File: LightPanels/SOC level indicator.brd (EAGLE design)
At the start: 170 x 162.3 mm, 156 parts

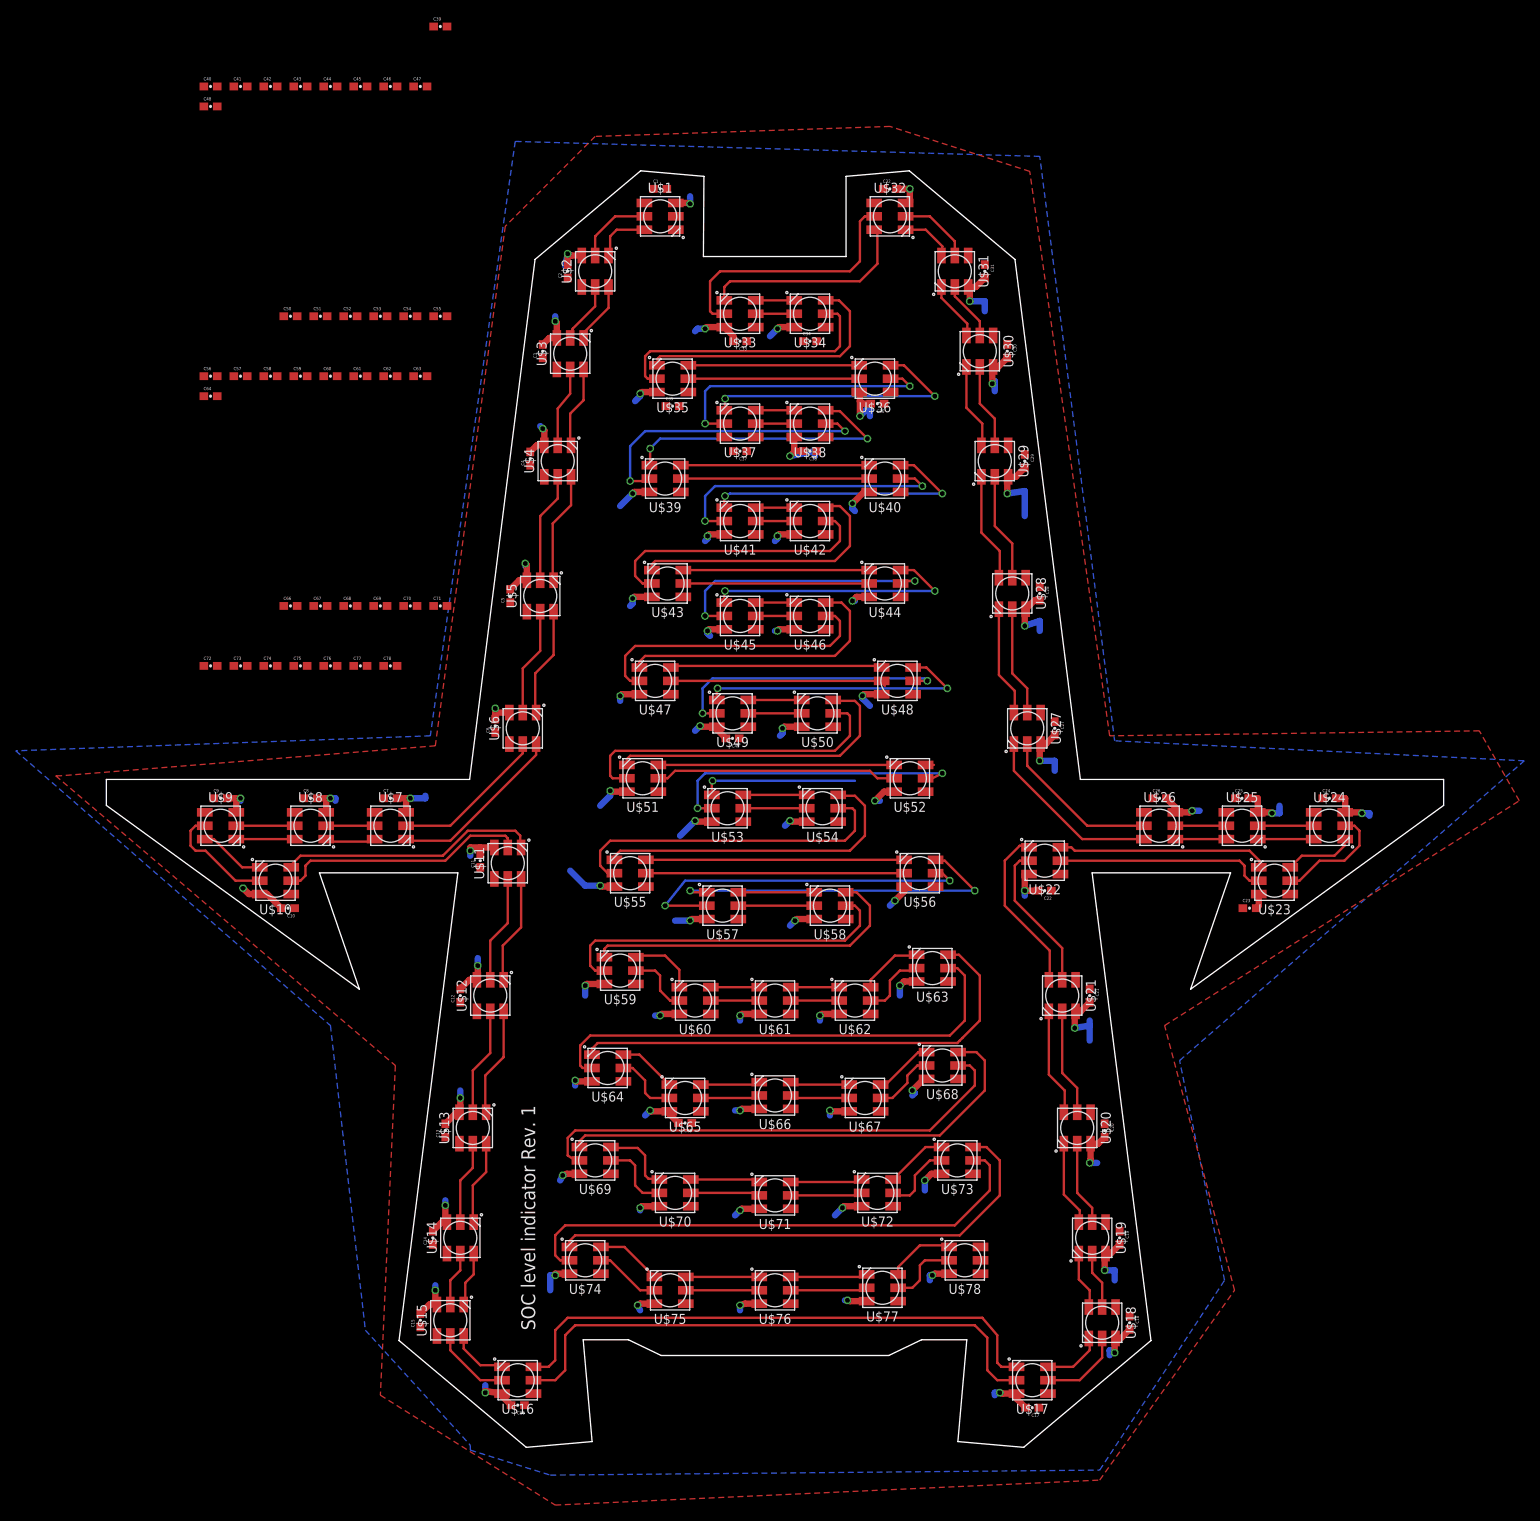
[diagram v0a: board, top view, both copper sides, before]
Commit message: No airwires
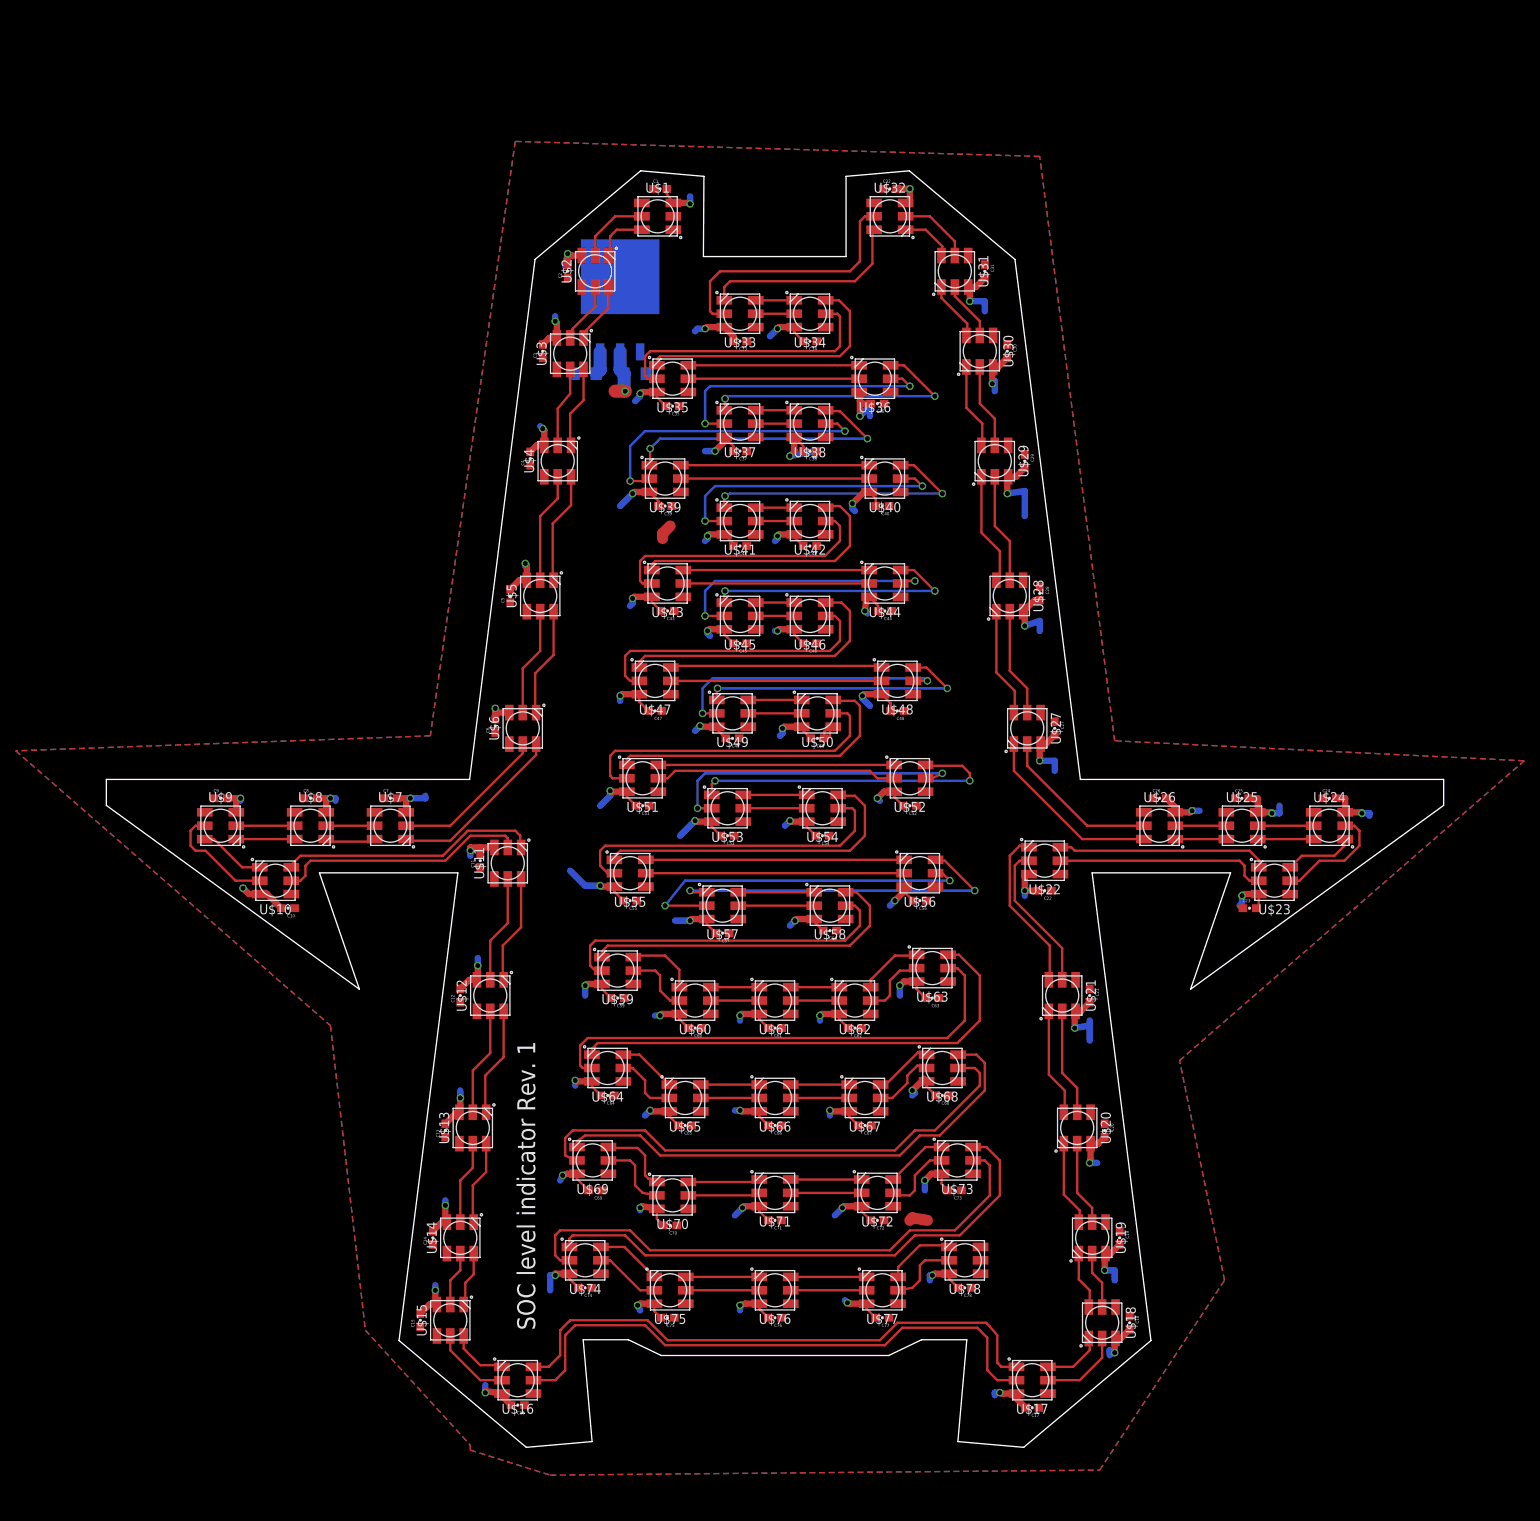
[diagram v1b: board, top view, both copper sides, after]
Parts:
- added C79, C84: 10uF, SparkFun-Capacitors:EIA3216
- added IC1: LM1084-ADJ, lm1084-adj-to263:TO263-3
- moved C48 116.3 mm to (15.6, 271.8), turned to 180 degrees
- moved C73 112.7 mm to (22.9, 210.8), turned to 180 degrees
- moved C56 112.1 mm to (18.4, 247.7), turned to 180 degrees
- moved C72 110.2 mm to (13.0, 207.0), turned to 180 degrees
- moved C78 107.6 mm to (24.1, 198.4), turned to 180 degrees
- moved C77 106.2 mm to (13.7, 194.6), turned to 180 degrees
- moved C63 102.4 mm to (20.0, 235.3), turned to 180 degrees
- moved C64 102.2 mm to (-21.3, 222.9), turned to 180 degrees
- moved C62 101.8 mm to (10.2, 231.5), turned to 180 degrees
- moved C40 100.7 mm to (13.7, 297.8), turned to 180 degrees
- moved C76 100.3 mm to (0.00, 194.6), turned to 180 degrees
- moved C58 100.1 mm to (6.99, 243.8), turned to 180 degrees
- moved C61 98.2 mm to (0.00, 231.5), turned to 180 degrees
- moved C68 97.6 mm to (21.3, 222.9), turned to 180 degrees
- moved C44 97.0 mm to (14.0, 284.5), turned to 180 degrees
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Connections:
- new net +12V: C84.A, IC1.3
- net +5V: now also C79.A, IC1.2
- net GND: now also C79.C, C84.C
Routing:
- net GND: track 351.8 -> 454.9 mm, vias 76 -> 78
- net N$108: track 21.0 -> 41.4 mm, vias 1 -> 2
- net +5V: track 0.00 -> 15.7 mm, vias 0 -> 1
- net N$139: track 62.7 -> 66.0 mm
- net +12V: track 0.00 -> 2.99 mm
- net N$142: track 67.8 -> 70.3 mm
- net N$141: track 66.4 -> 68.7 mm
- net N$140: track 62.6 -> 64.6 mm
- net N$62: track 72.2 -> 74.1 mm
- net N$61: track 71.0 -> 72.1 mm
- net N$82: track 35.5 -> 34.6 mm
- net N$93: track 27.0 -> 26.2 mm
- net N$133: track 9.55 -> 10.3 mm
- net N$86: track 27.5 -> 26.8 mm
- net N$109: track 10.6 -> 9.95 mm
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
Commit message: SOC level indicator
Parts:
- added PAD1, PAD2, PAD3, PAD4: WIREPADSMD5-2,5, wirepad:5-2,5
- moved C79 203.9 mm to (94.6, 144.5), turned to 270 degrees
- moved IC1 203.8 mm to (89.5, 151.1)
- moved C84 198.9 mm to (78.7, 144.5)
- moved C2 187.3 mm to (46.0, 154.9)
- moved C24 187.3 mm to (142.9, 87.9)
- moved C25 187.3 mm to (131.8, 87.9)
- moved C26 187.3 mm to (121.3, 87.9)
- moved C31 187.3 mm to (99.1, 154.9)
- moved C4 187.3 mm to (41.3, 131.1)
- moved C41 187.3 mm to (67.9, 120.0)
- moved C42 187.3 mm to (76.8, 120.0)
- moved C43 187.3 mm to (58.7, 111.8)
- moved C44 187.3 mm to (86.4, 111.8)
- moved C45 187.3 mm to (67.9, 107.6)
- moved C46 187.3 mm to (76.8, 107.6)
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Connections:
- new net N$149: PAD1.1, U$1.4
- new net N$150: PAD2.1, U$1.5
- net +12V: now also PAD3.1
- net GND: now also PAD4.1
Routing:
- net N$150: track 0.00 -> 17.9 mm, vias 0 -> 1
- net +12V: track 2.99 -> 14.6 mm
- net N$149: track 0.00 -> 10.7 mm, vias 0 -> 1
- net +5V: track 15.7 -> 19.1 mm
- net N$90: track 33.6 -> 34.9 mm
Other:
- board size 170 x 162.3 mm -> 161.2 x 162.3 mm
